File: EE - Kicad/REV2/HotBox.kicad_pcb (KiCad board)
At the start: 2 copper layers, 100 x 100 mm, 33 parts, among them J1 Conn_01x02, J2 Conn_01x01, J3 Conn_01x01, M1 Fan_4pin, M2 Fan, Q1 BSC028N06LS3, Q2 PUMH11, Q4 PUMD3,115, SW1 SW_Push_4PIN, SW2 SW_Push_4PIN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

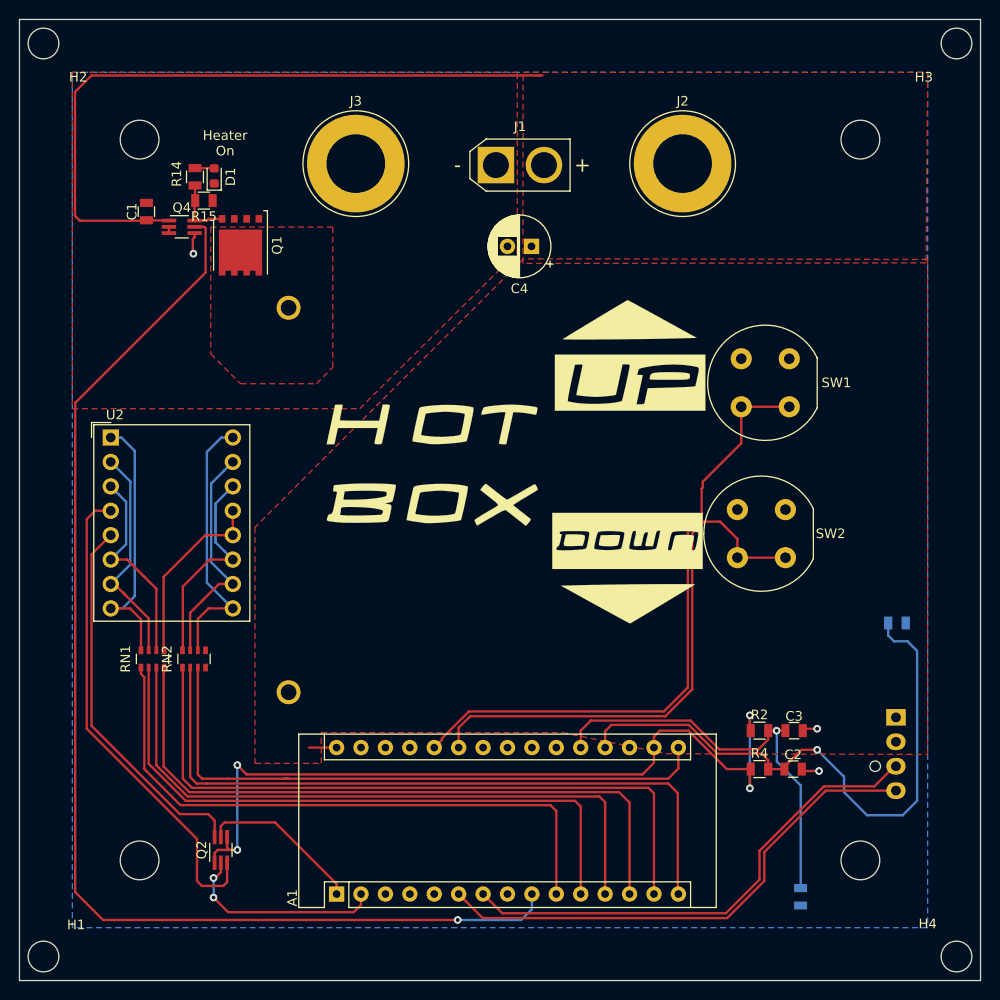
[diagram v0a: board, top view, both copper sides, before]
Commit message: Committing 2nd REV.  Update PCB to fix issues with REV1.  Reduce mechanical size.
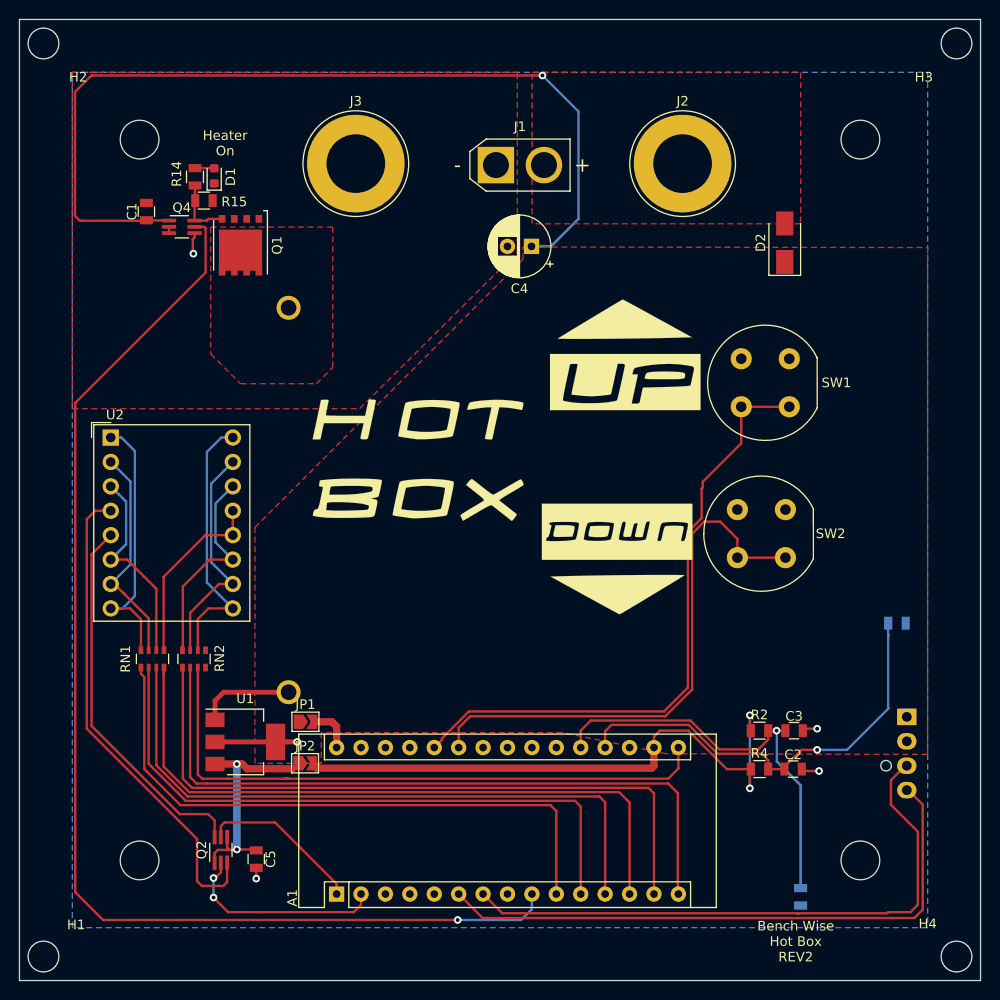
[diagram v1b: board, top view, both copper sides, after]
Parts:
- added C5: 0.1uF, AEvan:0805_C, F.Cu at (121.5, 131.7)
- added D2: D, Diode_SMD:D_SMA, F.Cu at (176.5, 67.6)
- added JP1: SolderJumper_2_Open, Jumper:SolderJumper-2_P1.3mm_Open_TrianglePad1.0x1.5mm, F.Cu at (126.6, 117.4)
- added JP2: SolderJumper_2_Open, Jumper:SolderJumper-2_P1.3mm_Open_TrianglePad1.0x1.5mm, F.Cu at (126.6, 121.7)
- added U1: UA78M33CDCYR, Package_TO_SOT_SMD:SOT-223-3_TabPin2, F.Cu at (120.4, 119.5)
- Q2: value PUMH11 -> PUMB11,115
- moved G*** 1.55 mm to (138.3, 90.2)
- moved G*** 1.44 mm to (159.1, 100.6)
- moved M1 1.13 mm to (189.2, 116.9)
- moved G*** 0.51 mm to (159.9, 79.1)
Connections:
- A1 pad 17: +3V3 -> Net-(A1-Pad17)
- A1 pad 30: +12V -> Net-(A1-Pad30)
- J1 pad 2: +12V -> Net-(D2-Pad2)
- J2 pad 1: +12V -> Net-(D2-Pad2)
- R2 pad 1: +3V3 -> Net-(A1-Pad17)
- R4 pad 1: +3V3 -> Net-(A1-Pad17)
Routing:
- net Net-(A1-Pad17): track 0.00 -> 62.1 mm, vias 0 -> 2
- net +3V3: track 84.0 -> 25.0 mm, vias 4 -> 2
- net +12V: track 75.1 -> 104.8 mm, vias 0 -> 1
- net Net-(A1-Pad19): track 62.8 -> 45.5 mm
- net Net-(A1-Pad7): track 51.9 -> 63.1 mm
- net GND: track 5.70 -> 15.4 mm, vias 3 -> 5
- net Net-(A1-Pad6): track 53.8 -> 62.9 mm
- net Net-(A1-Pad30): track 0.00 -> 4.79 mm
- added copper zone on F.Cu, net Net-(D2-Pad2)
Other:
- board text added: "Bench Wise Hot Box REV2"
